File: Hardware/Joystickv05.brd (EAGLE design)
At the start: 100 x 48.9 mm, 58 parts, among them J1 AVR_SPI_PRG_6PTH, U1 JOYSTICKPTH, U3 V_REG_MIC5219SMD, U4 MCP73831

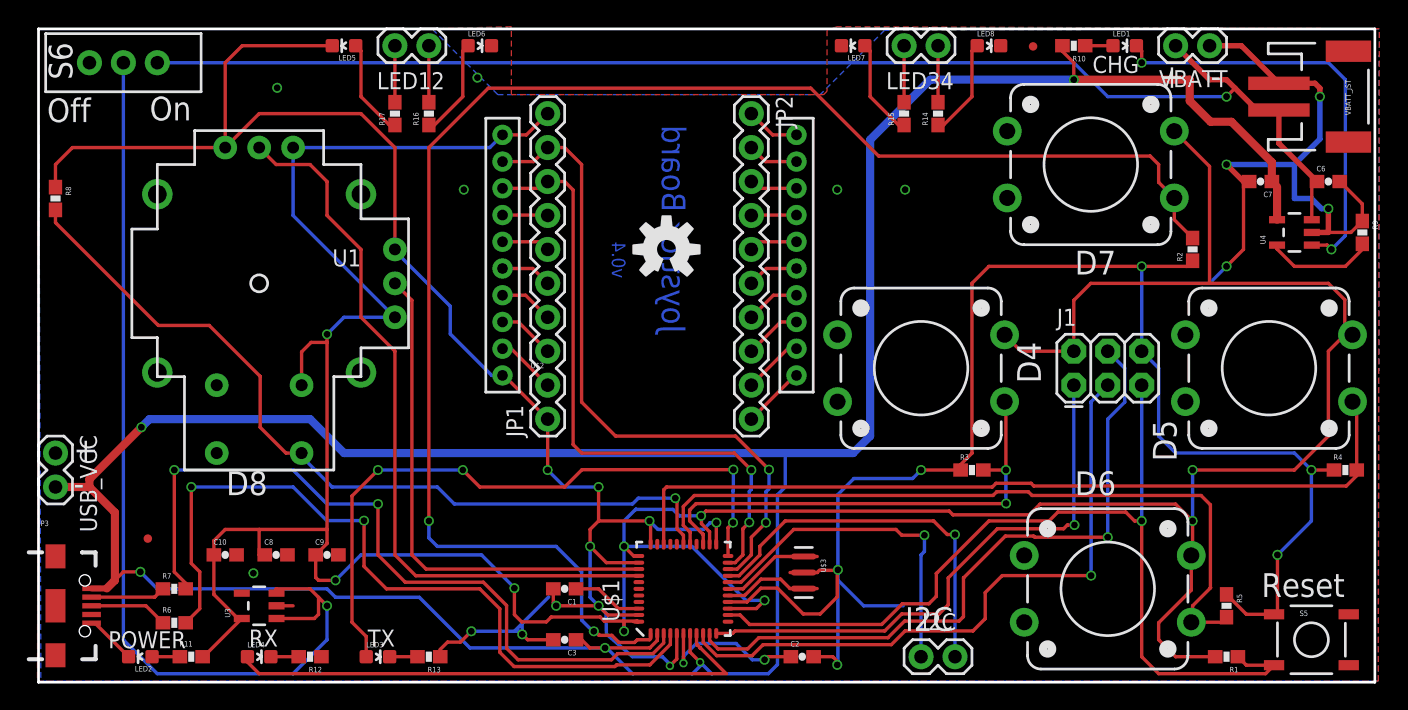
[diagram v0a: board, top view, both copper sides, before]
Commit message: Pre-review
V05.  This version has standoffs and is ready for a few comments before
bringing to engineering review
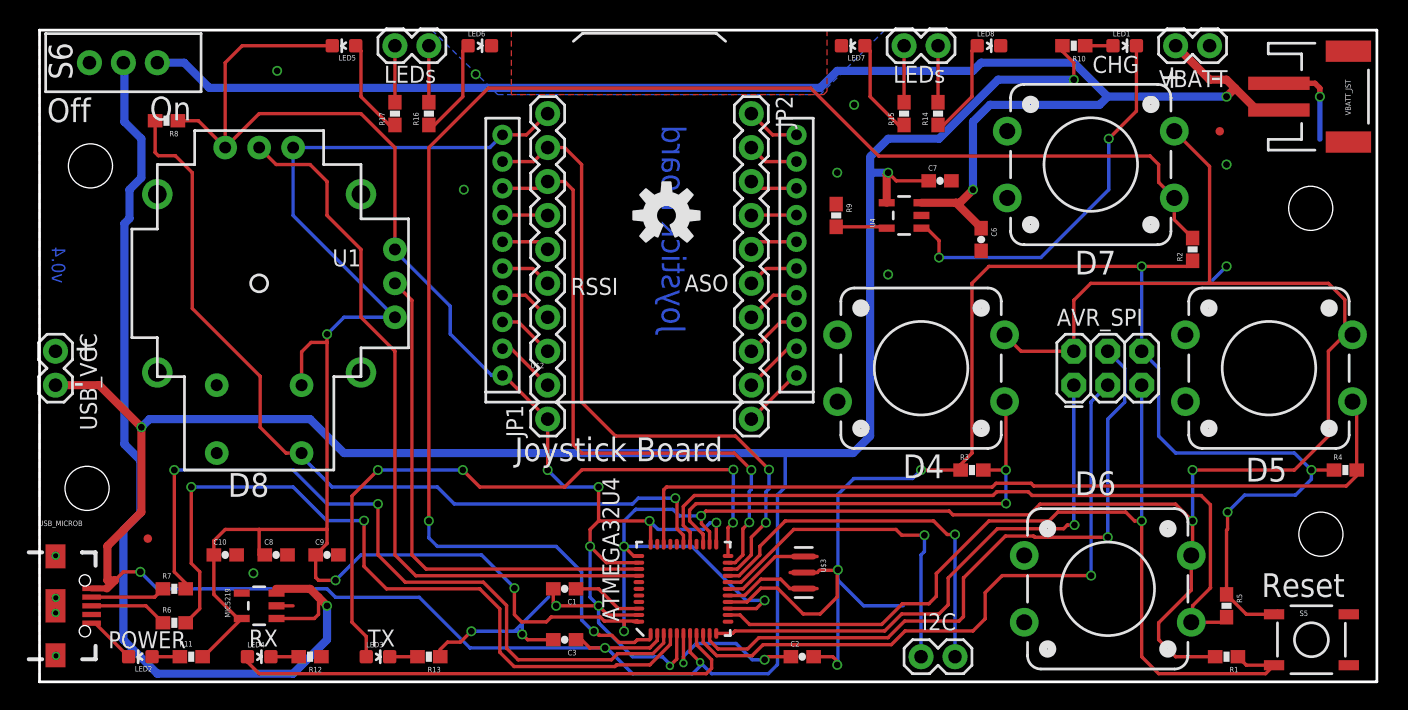
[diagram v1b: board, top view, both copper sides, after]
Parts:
- added STANDOFF1, STANDOFF2, STANDOFF3, STANDOFF4: STAND-OFF, SparkFun-Electromechanical:STAND-OFF
- U$2: value XBEE-1B1 -> XBEE-1B2; device SparkFun-RF:XBEE-1 -> SparkFun-RF:XBEE-SILK
- moved R9 39.4 mm to (59.6, 34.9)
- moved U4 29.2 mm to (64.7, 34.9)
- moved C6 26.3 mm to (70.5, 33.1), turned to 270 degrees
- moved C7 24.0 mm to (67.4, 37.5), turned to 0 degrees
- moved FID2 15.3 mm to (88.3, 41.2)
- moved R8 10.1 mm to (9.50, 42.0), turned to 180 degrees
- moved USB_VCC 7.62 mm to (1.19, 24.7)
- moved LOGO1 2.54 mm to (46.9, 34.9)
- renumbered J1 to AVR_SPI, JP3 to USB_MICROB, U$1 to ATMEGA32U4, U3 to MIC5219
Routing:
- net GND: track 313.6 -> 267.5 mm
- net VBATT: track 101.2 -> 116.1 mm, vias 1 -> 2
- net USB_VCC: track 219.3 -> 207.0 mm, vias 5 -> 6
- net N$11: track 8.15 -> 3.82 mm
- net N$28: track 31.9 -> 29.4 mm
- net VIN: track 72.3 -> 74.4 mm
- net D8: track 62.3 -> 64.4 mm
- net N$29: track 40.6 -> 38.8 mm
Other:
- board size 100 x 48.9 mm -> 100.1 x 48.8 mm
- board text added: "3.7V Lipo"
- board text added: "ASO"
- board text added: "Battery"
- board text added: "D2"
- board text added: "D3"
- board text added: "LEDs"
- board text added: "RSSI"
- board text added: "USB Power"
- board text removed: "I2C"
